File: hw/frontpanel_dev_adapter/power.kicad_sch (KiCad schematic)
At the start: 44 parts, among them J201 KLD-0202-A, J202 Conn_WR-FAST_01x04, J203 Molex_MicroFit_30-43045-0421, Q201 AO4407A, U201 TPS54332DDA, U202 TLV1117LV30DCY, U203 TLV1117LV30DCY

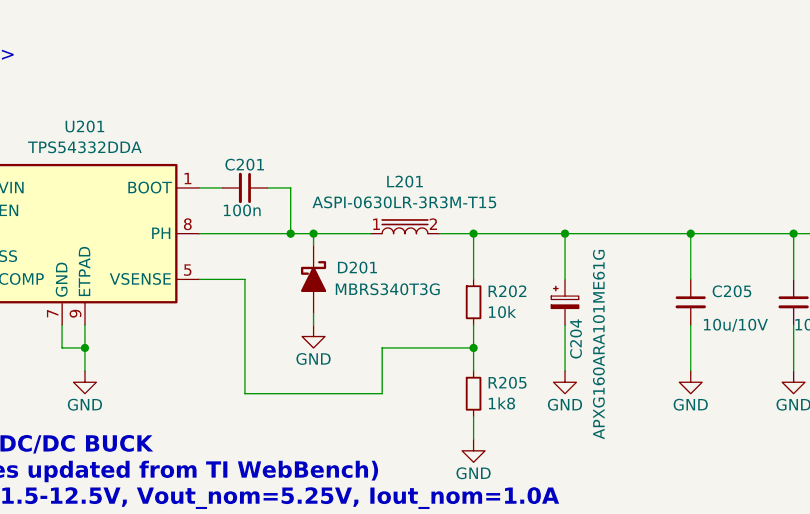
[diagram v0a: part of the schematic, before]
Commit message: Various boards & schematics (auto-)updated to Kicad-v8
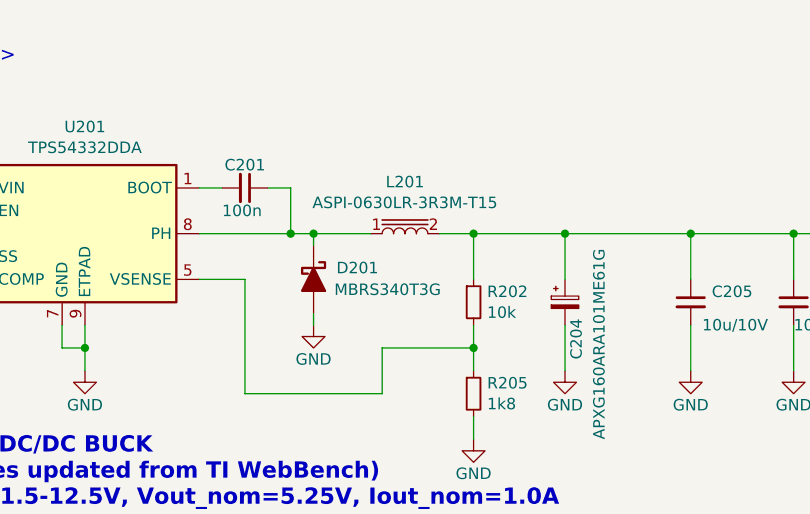
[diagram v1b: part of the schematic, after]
